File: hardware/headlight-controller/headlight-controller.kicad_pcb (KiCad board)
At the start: 2 copper layers, 78 x 52.5 mm, 43 parts, among them J1 Conn_ARM_JTAG_SWD_10, J2 776180-1, J3 BOOT, K1 SRD-05VDC-SL-C, K2 SRD-05VDC-SL-C, Q1 S8050, Q2 S8050, U1 AMS1117-3.3, U2 AMS1117-5.0, U3 STM32F103C8Tx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

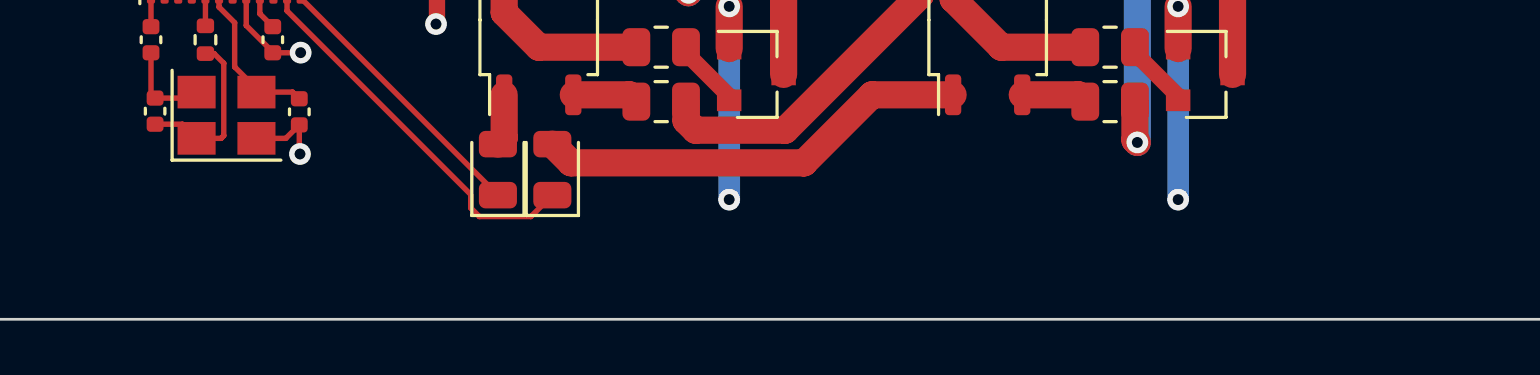
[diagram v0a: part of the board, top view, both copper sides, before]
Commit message: Restructure project
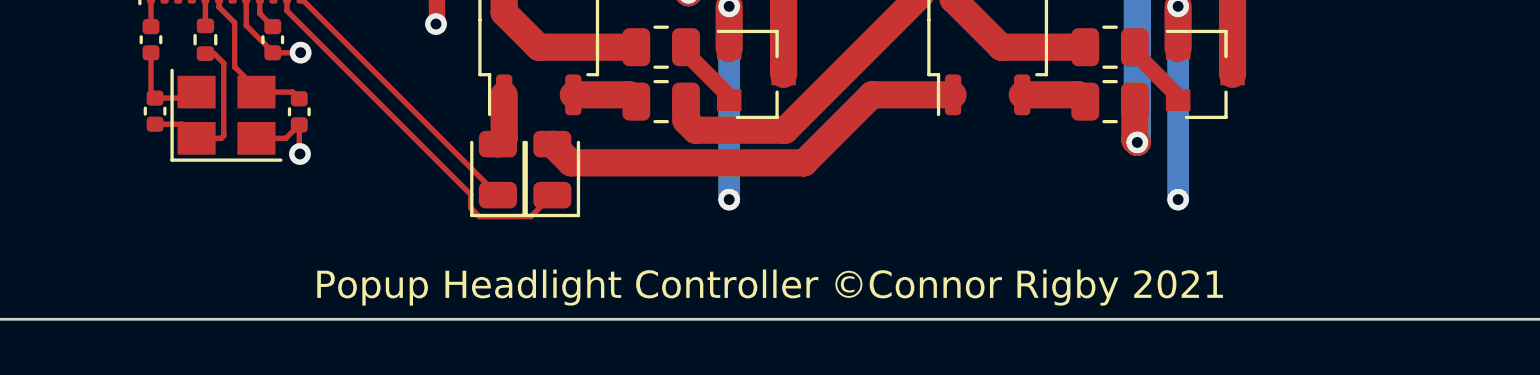
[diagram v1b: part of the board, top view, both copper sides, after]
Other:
- board text added: "Popup Headlight Controller ©Connor Rigby 2021"
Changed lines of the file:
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@@
   (general
     (thickness 1.6)
-    (drawings 8)
+    (drawings 9)
     (tracks 411)
     (zones 0)
@@
   )
   (setup
-    (last_trace_width 0.6)
+    (last_trace_width 0.25)
     (user_trace_width 0.2)
     (user_trace_width 0.4)
@@
       (effects (font (size 1 1) (thickness 0.15)))
     )
-    (fp_text user %R (at 0 0 90) (layer F.Fab)
-      (effects (font (size 0.26 0.26) (thickness 0.04)))
-    )
     (fp_line (start -0.525 0.27) (end -0.525 -0.27) (layer F.Fab) (width 0.1))
     (fp_line (start -0.525 -0.27) (end 0.525 -0.27) (layer F.Fab) (width 0.1))
@@
     (fp_line (start 0.93 -0.47) (end 0.93 0.47) (layer F.CrtYd) (width 0.05))
     (fp_line (start 0.93 0.47) (end -0.93 0.47) (layer F.CrtYd) (width 0.05))
+    (fp_text user %R (at 0 0 90) (layer F.Fab)
+      (effects (font (size 0.26 0.26) (thickness 0.04)))
+    )
     (pad 2 smd roundrect (at 0.51 0 270) (size 0.54 0.64) (layers F.Cu F.Paste F.Mask) (roundrect_rratio 0.25)
       (net 37 "Net-(R9-Pad2)"))
@@
     (fp_text value 100K (at 0 1.17 90) (layer F.Fab)
       (effects (font (size 1 1) (thickness 0.15)))
-    )
-    (fp_text user %R (at 0 0 90) (layer F.Fab)
-      (effects (font (size 0.26 0.26) (thickness 0.04)))
     )
     (fp_line (start -0.525 0.27) (end -0.525 -0.27) (layer F.Fab) (width 0.1))
@@
     (fp_line (start 0.93 -0.47) (end 0.93 0.47) (layer F.CrtYd) (width 0.05))
     (fp_line (start 0.93 0.47) (end -0.93 0.47) (layer F.CrtYd) (width 0.05))
+    (fp_text user %R (at 0 0 90) (layer F.Fab)
+      (effects (font (size 0.26 0.26) (thickness 0.04)))
+    )
     (pad 2 smd roundrect (at 0.51 0 90) (size 0.54 0.64) (layers F.Cu F.Paste F.Mask) (roundrect_rratio 0.25)
       (net 32 "Net-(J3-Pad4)"))
@@
     (fp_text value 1M (at 0 1.17 90) (layer F.Fab)
       (effects (font (size 1 1) (thickness 0.15)))
-    )
-    (fp_text user %R (at 0 0 90) (layer F.Fab)
-      (effects (font (size 0.26 0.26) (thickness 0.04)))
     )
     (fp_line (start -0.525 0.27) (end -0.525 -0.27) (layer F.Fab) (width 0.1))
@@
     (fp_line (start 0.93 -0.47) (end 0.93 0.47) (layer F.CrtYd) (width 0.05))
     (fp_line (start 0.93 0.47) (end -0.93 0.47) (layer F.CrtYd) (width 0.05))
+    (fp_text user %R (at 0 0 90) (layer F.Fab)
+      (effects (font (size 0.26 0.26) (thickness 0.04)))
+    )
     (pad 2 smd roundrect (at 0.51 0 270) (size 0.54 0.64) (layers F.Cu F.Paste F.Mask) (roundrect_rratio 0.25)
       (net 26 "Net-(C4-Pad1)"))
@@
     (fp_text value 100K (at 0 1.17 90) (layer F.Fab)
       (effects (font (size 1 1) (thickness 0.15)))
-    )
-    (fp_text user %R (at 0 0 90) (layer F.Fab)
-      (effects (font (size 0.26 0.26) (thickness 0.04)))
     )
     (fp_line (start -0.525 0.27) (end -0.525 -0.27) (layer F.Fab) (width 0.1))
@@
     (fp_line (start 0.93 -0.47) (end 0.93 0.47) (layer F.CrtYd) (width 0.05))
     (fp_line (start 0.93 0.47) (end -0.93 0.47) (layer F.CrtYd) (width 0.05))
+    (fp_text user %R (at 0 0 90) (layer F.Fab)
+      (effects (font (size 0.26 0.26) (thickness 0.04)))
+    )
     (pad 2 smd roundrect (at 0.51 0 270) (size 0.54 0.64) (layers F.Cu F.Paste F.Mask) (roundrect_rratio 0.25)
       (net 34 /BOOT0))
@@
     )
     (fp_text value BOOT (at 1.27 7.41) (layer F.Fab)
-      (effects (font (size 1 1) (thickness 0.15)))
-    )
-    (fp_text user %R (at 1.27 2.54 90) (layer F.Fab)
       (effects (font (size 1 1) (thickness 0.15)))
     )
@@
     (fp_line (start 4.35 6.85) (end 4.35 -1.8) (layer F.CrtYd) (width 0.05))
     (fp_line (start 4.35 -1.8) (end -1.8 -1.8) (layer F.CrtYd) (width 0.05))
+    (fp_text user %R (at 1.27 2.54 90) (layer F.Fab)
+      (effects (font (size 1 1) (thickness 0.15)))
+    )
     (pad 6 thru_hole oval (at 2.54 5.08) (size 1.7 1.7) (drill 1) (layers *.Cu *.Mask)
       (net 1 GND))
@@
     (fp_text value 100n (at 0 1.16 90) (layer F.Fab)
       (effects (font (size 1 1) (thickness 0.15)))
-    )
-    (fp_text user %R (at 0 0 90) (layer F.Fab)
-      (effects (font (size 0.25 0.25) (thickness 0.04)))
     )
     (fp_line (start -0.5 0.25) (end -0.5 -0.25) (layer F.Fab) (width 0.1))
@@
     (fp_line (start 0.91 -0.46) (end 0.91 0.46) (layer F.CrtYd) (width 0.05))
     (fp_line (start 0.91 0.46) (end -0.91 0.46) (layer F.CrtYd) (width 0.05))
+    (fp_text user %R (at 0 0 90) (layer F.Fab)
+      (effects (font (size 0.25 0.25) (thickness 0.04)))
+    )
     (pad 2 smd roundrect (at 0.48 0 270) (size 0.56 0.62) (layers F.Cu F.Paste F.Mask) (roundrect_rratio 0.25)
       (net 1 GND))
@@
     (fp_text value 100n (at 0 1.16 90) (layer F.Fab)
       (effects (font (size 1 1) (thickness 0.15)))
-    )
-    (fp_text user %R (at 0 0 90) (layer F.Fab)
-      (effects (font (size 0.25 0.25) (thickness 0.04)))
     )
     (fp_line (start -0.5 0.25) (end -0.5 -0.25) (layer F.Fab) (width 0.1))
@@
     (fp_line (start 0.91 -0.46) (end 0.91 0.46) (layer F.CrtYd) (width 0.05))
     (fp_line (start 0.91 0.46) (end -0.91 0.46) (layer F.CrtYd) (width 0.05))
+    (fp_text user %R (at 0 0 90) (layer F.Fab)
+      (effects (font (size 0.25 0.25) (thickness 0.04)))
+    )
     (pad 2 smd roundrect (at 0.48 0 90) (size 0.56 0.62) (layers F.Cu F.Paste F.Mask) (roundrect_rratio 0.25)
       (net 1 GND))
@@
       (effects (font (size 1 1) (thickness 0.15)))
     )
-    (fp_text user %R (at 0 0 90) (layer F.Fab)
-      (effects (font (size 0.98 0.98) (thickness 0.15)))
-    )
     (fp_line (start 0 2.56) (end 1.95 2.56) (layer F.SilkS) (width 0.12))
     (fp_line (start 0 2.56) (end -1.95 2.56) (layer F.SilkS) (width 0.12))
@@
     (fp_line (start 3.7 2.7) (end 3.7 -2.7) (layer F.CrtYd) (width 0.05))
     (fp_line (start 3.7 -2.7) (end -3.7 -2.7) (layer F.CrtYd) (width 0.05))
+    (fp_text user %R (at 0 0 90) (layer F.Fab)
+      (effects (font (size 0.98 0.98) (thickness 0.15)))
+    )
     (pad 1 smd roundrect (at -2.475 -1.905 90) (size 1.95 0.6) (layers F.Cu F.Paste F.Mask) (roundrect_rratio 0.25)
       (net 38 /CAN_TX))
@@
     )
     (fp_text value STM32F103C8Tx (at 0 5.85 90) (layer F.Fab)
-      (effects (font (size 1 1) (thickness 0.15)))
-    )
-    (fp_text user %R (at 0 0 90) (layer F.Fab)
       (effects (font (size 1 1) (thickness 0.15)))
     )
@@
     (fp_line (start 3.75 3.15) (end 5.15 3.15) (layer F.CrtYd) (width 0.05))
     (fp_line (start 5.15 3.15) (end 5.15 0) (layer F.CrtYd) (width 0.05))
+    (fp_text user %R (at 0 0 90) (layer F.Fab)
+      (effects (font (size 1 1) (thickness 0.15)))
+    )
     (pad 1 smd roundrect (at -4.1625 -2.75 90) (size 1.475 0.3) (layers F.Cu F.Paste F.Mask) (roundrect_rratio 0.25)
       (net 3 +3V3))
@@
     (pad A1 thru_hole rect (at -6.1 -6 90) (size 1.98 1.98) (drill 1.32) (layers *.Cu *.Mask)
       (net 4 +5V))
-    (model ${KIPRJMOD}/library/SRD-05VDC-SL-C.pretty/SRD-05VDC-SL-C.step
+    (model ${KIPRJMOD}/../_library/SRD-05VDC-SL-C.pretty/SRD-05VDC-SL-C.step
       (offset (xyz 9 7.5 0))
       (scale (xyz 1 1 1))
@@
     (pad A1 thru_hole rect (at -6.1 -6 90) (size 1.98 1.98) (drill 1.32) (layers *.Cu *.Mask)
       (net 4 +5V))
-    (model ${KIPRJMOD}/library/SRD-05VDC-SL-C.pretty/SRD-05VDC-SL-C.step
+    (model ${KIPRJMOD}/../_library/SRD-05VDC-SL-C.pretty/SRD-05VDC-SL-C.step
       (offset (xyz 9 7.5 0))
       (scale (xyz 1 1 1))
@@
     (fp_text value 776180-1 (at -20.292765 33.598915) (layer F.Fab)
       (effects (font (size 1.402181 1.402181) (thickness 0.15)))
-    )
-    (fp_text user PCB~EDGE (at -4.83273 9.4031) (layer F.Fab)
-      (effects (font (size 1.401953 1.401953) (thickness 0.15)))
     )
     (fp_circle (center -21.97 -7.62) (end -21.77 -7.62) (layer F.SilkS) (width 0.4))
@@
     (fp_line (start -38.45 9.5) (end -38.45 11.8) (layer F.Fab) (width 0.1524))
     (fp_line (start -38.45 -6.05) (end -38.45 9.5) (layer F.Fab) (width 0.1524))
+    (fp_text user PCB~EDGE (at -4.83273 9.4031) (layer F.Fab)
+      (effects (font (size 1.401953 1.401953) (thickness 0.15)))
+    )
     (pad None np_thru_hole circle (at -28.5 0.5 180) (size 2.85 2.85) (drill 2.85) (layers *.Cu *.Mask))
     (pad 1 thru_hole rect (at -22 -4 180) (size 2.625 2.625) (drill 1.75) (layers *.Cu *.Mask)
@@
     (pad 35 thru_hole circle (at 22 4 180) (size 2.625 2.625) (drill 1.75) (layers *.Cu *.Mask)
       (net 17 /CANH))
-    (model ${KIPRJMOD}/library/Connector_Automotive.pretty/776180-1.step
+    (model ${KIPRJMOD}/../_library/Connector_Automotive.pretty/776180-1.step
       (offset (xyz 0 -32 11.5))
       (scale (xyz 1 1 1))
@@
     (pad 10 smd rect (at 2.54 -1.78 90) (size 0.76 2.05) (layers F.Cu F.Paste F.Mask)
       (net 30 /JNTRST))
-    (model ${KIPRJMOD}/library/Connector_SWD.pretty/2002122100010c4lf.stp
+    (model ${KIPRJMOD}/../_library/Connector_SWD.pretty/2002122100010c4lf.stp
       (at (xyz 0 0 0))
       (scale (xyz 1 1 1))
@@
     )
   )
+  (gr_text "Popup Headlight Controller ©Connor Rigby 2021" (at 58 93.25) (layer F.SilkS)
+    (effects (font (size 1 1) (thickness 0.15)))
+  )
   (gr_arc (start 23 90.5) (end 19 90.5) (angle -90) (layer Edge.Cuts) (width 0.1))
